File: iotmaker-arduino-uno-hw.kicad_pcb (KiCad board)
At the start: 2 copper layers, 68.5 x 53.3 mm, 65 parts, among them J1 BARREL_JACK, J2 USB_A, J3 Servo, J5 Header module, J6 CONN_02X03, J7 Header Analog, J8 DHT, Q1 SI2301DS_GSD, SW1 RESET, SW2 SW_PUSH, U2 ATMEGA328P-AU, U3 LM358, U4 FAN1117A-3.3v, U5 FAN1117A-5.0v, U6 CH340E, Y1 16MHz_GND24

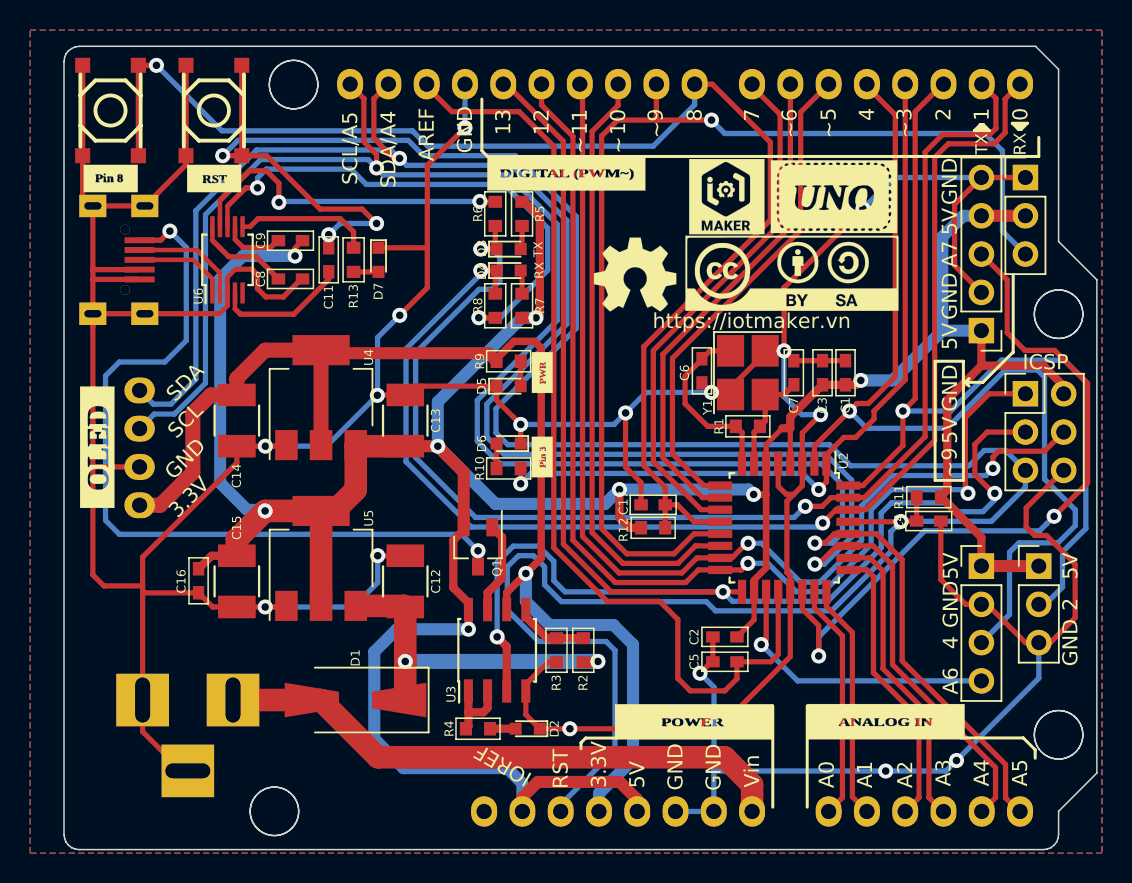
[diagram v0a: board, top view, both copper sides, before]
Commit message: change button pin8 to pin2 and header pin2 to pin7
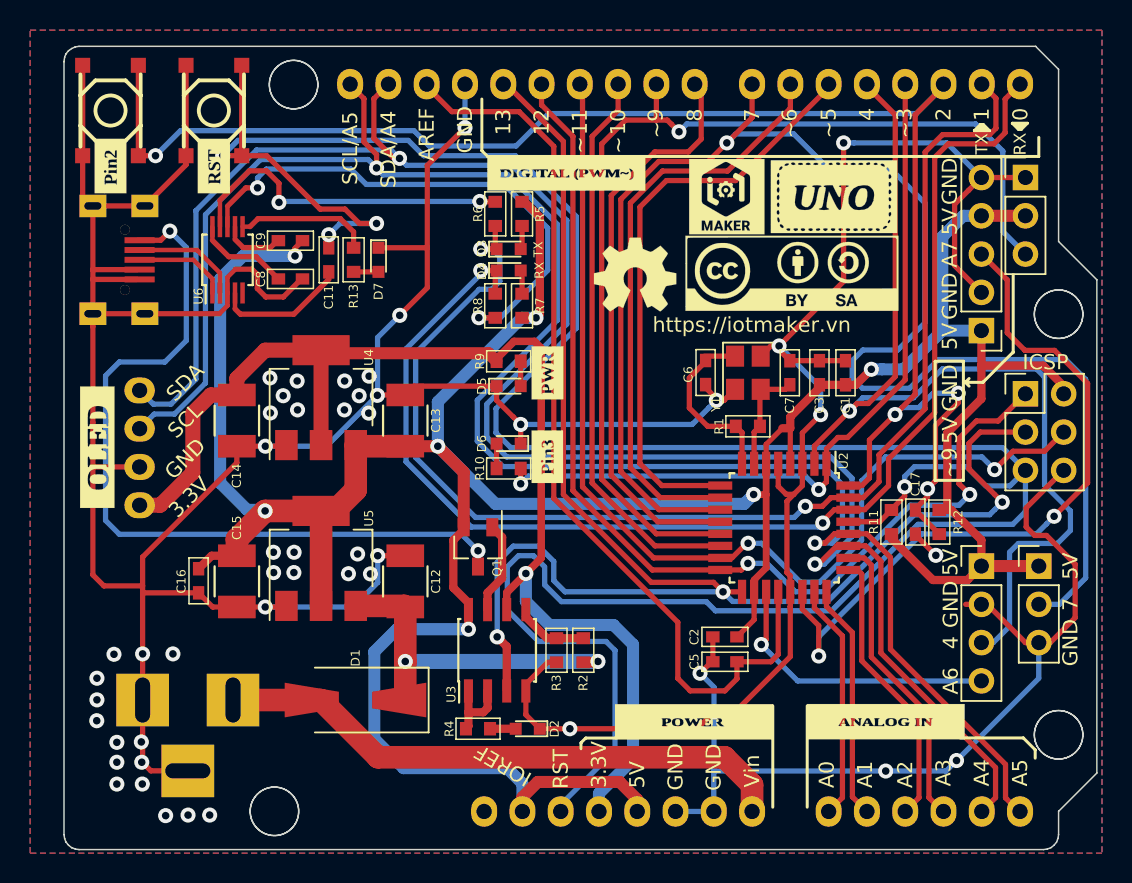
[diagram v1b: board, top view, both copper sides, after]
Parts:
- removed C4: 100nF, footprint:C_0603
- removed the G*** at (144.3, 103.3)
- added G***: LOGO, footprint:label-arduino-pin2, F.Cu at (115.7, 84.0)
- C9: value 100nF -> 0R
- J1: value BARREL_JACK -> BARREL_JACK_5.5x2.1
- R10: value 1k -> 560R
- Y1: footprint Crystals:Crystal_SMD_3225-4pin_3.2x2.5mm_HandSoldering -> Crystals:Crystal_SMD_3225-4pin_3.2x2.5mm
- moved G*** 34.4 mm to (144.7, 103.3), turned to 90 degrees
- moved R12 19.0 mm to (170.7, 107.6), turned to 90 degrees
- moved C17 17.4 mm to (169.1, 107.6), turned to 90 degrees
- moved R11 2.98 mm to (167.5, 107.6), turned to 270 degrees
- moved G*** 0.77 mm to (122.6, 84.0), turned to 90 degrees
- moved G*** 0.34 mm to (144.7, 97.7)
- moved C6 0.27 mm to (155.2, 97.7)
- moved C7 0.27 mm to (160.8, 97.7)
- moved C3 0.20 mm to (162.7, 97.7)
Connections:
- C17 pad 2: PB0 -> PD2
- J8 pad 2: PD2 -> PD7
- R12 pad 1: PB0 -> PD2
- S1 pad 1: (no net) -> Net-(S1-Pad1)
- SW2 pad 1: PB0 -> PD2
- SW2 pad 2: PB0 -> PD2
- U6 pad 5: (no net) -> Net-(U6-Pad5)
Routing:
- net PD7: track 35.1 -> 103.3 mm, vias 0 -> 1
- net PB0: track 88.0 -> 38.4 mm, vias 1 -> 0
- net PD2: track 60.3 -> 108.1 mm, vias 1 -> 4
- net PC6/RESET: track 173.7 -> 182.0 mm
- net GND: track 361.1 -> 353.8 mm, vias 17 -> 49
- net PD5: track 32.9 -> 39.0 mm
- net PD6: track 33.2 -> 39.2 mm
- net +5V: track 224.4 -> 229.1 mm, vias 8 -> 7
- net PB4: track 73.8 -> 69.6 mm
- net PB1: track 73.3 -> 70.3 mm
- net PB2: track 40.3 -> 37.4 mm
- net PB5: track 102.6 -> 100.2 mm
- net AREF: track 63.4 -> 61.4 mm
- net PB3: track 70.8 -> 69.3 mm
- net PD4: track 67.5 -> 66.9 mm

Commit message: update gerber pcb & gerber 4 panel
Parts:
- moved G*** 0.13 mm to (163.6, 86.0)
